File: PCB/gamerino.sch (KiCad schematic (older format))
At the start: 47 parts, among them J1 USB_B_Micro, J2 LT2, J3 RT2, P1 JOY1, P2 JOY2, P3 ICSP, P4 AUX, SW1 HATSWITCH, SW10 OPTS, SW11 X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

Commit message: Update
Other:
- moved on the sheet: J2, JOY1, R4, SW9B
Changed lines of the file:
@@
 	7825 9925 7600 9925
 Wire Wire Line
-	7600 8075 7825 8075
+	7600 8175 7825 8175
 $Comp
 L gamerino-rescue:GND-power #PWR026
@@
 L gamerino-rescue:R-device R4
 U 1 1 60E4EB67
-P 9100 8700
-F 0 "R4" H 9171 8746 50  0000 L CNN
-F 1 "1K" H 9171 8655 50  0000 L CNN
-F 2 "Resistor_SMD:R_0603_1608Metric" V 9030 8700 30  0001 C CNN
-F 3 "" H 9100 8700 30  0000 C CNN
-F 4 "CRG0603F1K0" H 9100 8700 50  0001 C CNN "MPN"
-F 5 "TE" H 9100 8700 50  0001 C CNN "Manufacturer"
-F 6 "A106049CT-ND" H 9100 8700 50  0001 C CNN "Digikey"
-F 7 "279-CRG0603F1K0" H 9100 8700 50  0001 C CNN "Mouser"
-F 8 "213-2266" H 9100 8700 50  0001 C CNN "RS"
-F 9 "3399571" H 9100 8700 50  0001 C CNN "Farnell"
-	1    9100 8700
+P 9100 8800
+F 0 "R4" H 9171 8846 50  0000 L CNN
+F 1 "1K" H 9171 8755 50  0000 L CNN
+F 2 "Resistor_SMD:R_0603_1608Metric" V 9030 8800 30  0001 C CNN
+F 3 "" H 9100 8800 30  0000 C CNN
+F 4 "CRG0603F1K0" H 9100 8800 50  0001 C CNN "MPN"
+F 5 "TE" H 9100 8800 50  0001 C CNN "Manufacturer"
+F 6 "A106049CT-ND" H 9100 8800 50  0001 C CNN "Digikey"
+F 7 "279-CRG0603F1K0" H 9100 8800 50  0001 C CNN "Mouser"
+F 8 "213-2266" H 9100 8800 50  0001 C CNN "RS"
+F 9 "3399571" H 9100 8800 50  0001 C CNN "Farnell"
+	1    9100 8800
 	1    0    0    -1
 $EndComp
@@
 Text Label 10500 4950 0    50   ~ 0
 RT1
-Text Label 7600 8075 2    50   ~ 0
+Text Label 7600 8175 2    50   ~ 0
 LT2
 Text Label 7600 9925 2    50   ~ 0
@@
 L gamerino-rescue:+3.3V-power #PWR023
 U 1 1 6116AC53
-P 7825 7725
-F 0 "#PWR023" H 7825 7575 50  0001 C CNN
-F 1 "+3.3V" H 7840 7898 50  0000 C CNN
-F 2 "" H 7825 7725 50  0001 C CNN
-F 3 "" H 7825 7725 50  0001 C CNN
-	1    7825 7725
+P 7825 7825
+F 0 "#PWR023" H 7825 7675 50  0001 C CNN
+F 1 "+3.3V" H 7840 7998 50  0000 C CNN
+F 2 "" H 7825 7825 50  0001 C CNN
+F 3 "" H 7825 7825 50  0001 C CNN
+	1    7825 7825
 	-1   0    0    -1
 $EndComp
@@
 L gamerino-rescue:GND-power #PWR024
 U 1 1 6116B2BE
-P 7825 8500
-F 0 "#PWR024" H 7825 8250 50  0001 C CNN
-F 1 "GND" H 7830 8327 50  0000 C CNN
-F 2 "" H 7825 8500 50  0001 C CNN
-F 3 "" H 7825 8500 50  0001 C CNN
-	1    7825 8500
+P 7825 8600
+F 0 "#PWR024" H 7825 8350 50  0001 C CNN
+F 1 "GND" H 7830 8427 50  0000 C CNN
+F 2 "" H 7825 8600 50  0001 C CNN
+F 3 "" H 7825 8600 50  0001 C CNN
+	1    7825 8600
 	-1   0    0    -1
 $EndComp
 Wire Wire Line
-	7825 7725 7825 7975
-Wire Wire Line
-	7825 8175 7825 8500
+	7825 7825 7825 8075
+Wire Wire Line
+	7825 8275 7825 8600
 $Comp
 L gamerino-rescue:CONN_3-conn J2
 U 1 1 6116B2CB
-P 8175 8075
-F 0 "J2" H 8042 7739 50  0000 C CNN
-F 1 "LT2" H 8042 7830 50  0000 C CNN
-F 2 "gamerino:Molex_PicoBlade_53047-0310_1x03_P1.25mm_Vertical" H 8175 8075 50  0001 C CNN
-F 3 "" H 8175 8075 50  0001 C CNN
-F 4 "53047-0310" H 8175 8075 50  0001 C CNN "MPN"
-F 5 "Molex" H 8175 8075 50  0001 C CNN "Manufacturer"
-F 6 "WM1732-ND" H 8175 8075 50  0001 C CNN "Digikey"
-F 7 "538-53047-0310" H 8175 8075 50  0001 C CNN "Mouser"
-F 8 "319-1064" H 8175 8075 50  0001 C CNN "RS"
-F 9 "9732853" H 8175 8075 50  0001 C CNN "Farnell"
-	1    8175 8075
+P 8175 8175
+F 0 "J2" H 8042 7839 50  0000 C CNN
+F 1 "LT2" H 8042 7930 50  0000 C CNN
+F 2 "gamerino:Molex_PicoBlade_53047-0310_1x03_P1.25mm_Vertical" H 8175 8175 50  0001 C CNN
+F 3 "" H 8175 8175 50  0001 C CNN
+F 4 "53047-0310" H 8175 8175 50  0001 C CNN "MPN"
+F 5 "Molex" H 8175 8175 50  0001 C CNN "Manufacturer"
+F 6 "WM1732-ND" H 8175 8175 50  0001 C CNN "Digikey"
+F 7 "538-53047-0310" H 8175 8175 50  0001 C CNN "Mouser"
+F 8 "319-1064" H 8175 8175 50  0001 C CNN "RS"
+F 9 "9732853" H 8175 8175 50  0001 C CNN "Farnell"
+	1    8175 8175
 	1    0    0    1
 $EndComp
@@
 Connection ~ 14900 2950
 Wire Wire Line
-	9100 8450 9100 8325
-Wire Wire Line
-	9100 8950 9100 9075
+	9100 8550 9100 8425
+Wire Wire Line
+	9100 9050 9100 9175
 $Comp
 L gamerino-rescue:+3.3V-power #PWR0103
 U 1 1 60C0ACCD
-P 9100 7725
-F 0 "#PWR0103" H 9100 7575 50  0001 C CNN
-F 1 "+3.3V" H 9115 7898 50  0000 C CNN
-F 2 "" H 9100 7725 50  0001 C CNN
-F 3 "" H 9100 7725 50  0001 C CNN
-	1    9100 7725
+P 9100 7825
+F 0 "#PWR0103" H 9100 7675 50  0001 C CNN
+F 1 "+3.3V" H 9115 7998 50  0000 C CNN
+F 2 "" H 9100 7825 50  0001 C CNN
+F 3 "" H 9100 7825 50  0001 C CNN
+	1    9100 7825
 	1    0    0    -1
 $EndComp
@@
 L gamerino:TL1 SW9
 U 2 1 60C5CD0F
-P 8800 8075
-F 0 "SW9" V 8846 7597 50  0000 R CNN
-F 1 "HOME" V 8755 7597 50  0000 R CNN
-F 2 "gamerino:TL3265" H 8800 8225 50  0001 C CNN
-F 3 "" H 8800 8225 50  0001 C CNN
-F 4 "TL3265GQSCLR" H 8800 8075 50  0001 C CNN "MPN"
-F 5 "E-Switch" H 8800 8075 50  0001 C CNN "Manufacturer"
-F 6 "EG5518CT-ND" H 8800 8075 50  0001 C CNN "Digikey"
-F 7 "612-TL3265GQSCLR" H 8800 8075 50  0001 C CNN "Mouser"
-	2    8800 8075
+P 8800 8175
+F 0 "SW9" V 8846 7697 50  0000 R CNN
+F 1 "HOME" V 8755 7697 50  0000 R CNN
+F 2 "gamerino:TL3265" H 8800 8325 50  0001 C CNN
+F 3 "" H 8800 8325 50  0001 C CNN
+F 4 "TL3265GQSCLR" H 8800 8175 50  0001 C CNN "MPN"
+F 5 "E-Switch" H 8800 8175 50  0001 C CNN "Manufacturer"
+F 6 "EG5518CT-ND" H 8800 8175 50  0001 C CNN "Digikey"
+F 7 "612-TL3265GQSCLR" H 8800 8175 50  0001 C CNN "Mouser"
+	2    8800 8175
 	0    -1   -1   0
 $EndComp
 Wire Wire Line
-	9100 7825 9100 7725
+	9100 7925 9100 7825
 Wire Wire Line
 	14725 4325 14900 4325
@@
 L gamerino:RKJXU JOY1
 U 1 1 60AED526
-P 10725 7975
-F 0 "JOY1" H 10650 8400 50  0000 C CNN
-F 1 "RKJXU" H 10650 8300 50  0000 C CNN
-F 2 "gamerino:RKJXU" H 10050 7975 50  0001 C CNN
-F 3 "" H 10050 7975 50  0001 C CNN
-F 4 "RKJXU1210006" H 10725 7975 50  0001 C CNN "MPN"
-F 5 "ALPS Alpine" H 10725 7975 50  0001 C CNN "Manufacturer"
-F 6 "688-RKJXU1210006" H 10725 7975 50  0001 C CNN "Mouser"
-	1    10725 7975
+P 10725 8050
+F 0 "JOY1" H 10650 8475 50  0000 C CNN
+F 1 "RKJXU" H 10650 8375 50  0000 C CNN
+F 2 "gamerino:RKJXU" H 10050 8050 50  0001 C CNN
+F 3 "" H 10050 8050 50  0001 C CNN
+F 4 "RKJXU1210006" H 10725 8050 50  0001 C CNN "MPN"
+F 5 "ALPS Alpine" H 10725 8050 50  0001 C CNN "Manufacturer"
+F 6 "688-RKJXU1210006" H 10725 8050 50  0001 C CNN "Mouser"
+	1    10725 8050
 	1    0    0    -1
 $EndComp
@@
 NoConn ~ 10925 10300
 NoConn ~ 11200 9600
-NoConn ~ 11200 7750
-NoConn ~ 10050 7975
-NoConn ~ 10050 8175
-NoConn ~ 10925 8450
-Wire Wire Line
-	9100 9075 8900 9075
-Text Label 8900 9075 2    50   ~ 0
+NoConn ~ 11200 7825
+NoConn ~ 10050 8050
+NoConn ~ 10050 8250
+NoConn ~ 10925 8525
+Wire Wire Line
+	9100 9175 8900 9175
+Text Label 8900 9175 2    50   ~ 0
 LHOME
 Text Label 4725 4550 0    50   ~ 0

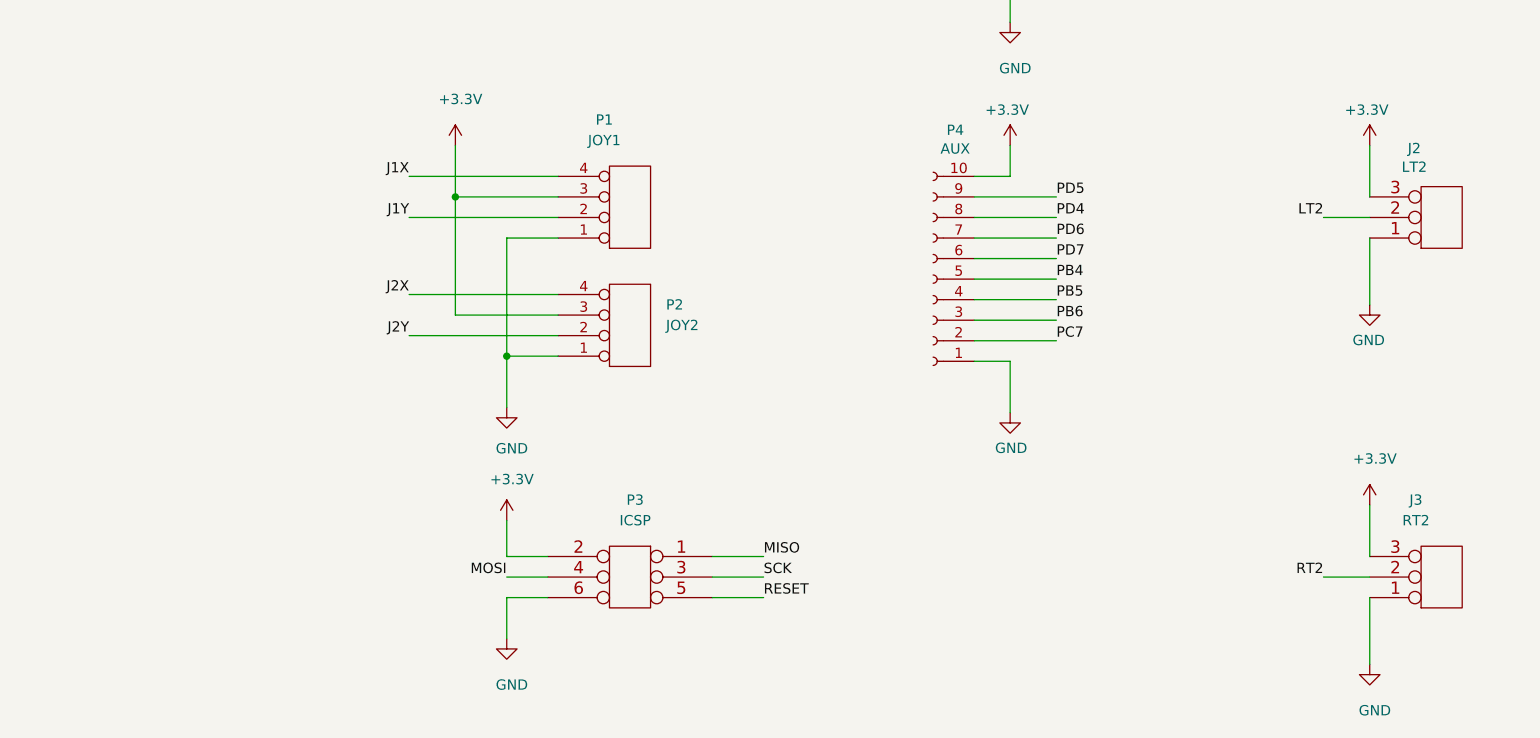
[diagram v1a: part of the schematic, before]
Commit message: Add ESD protections to analog inputs
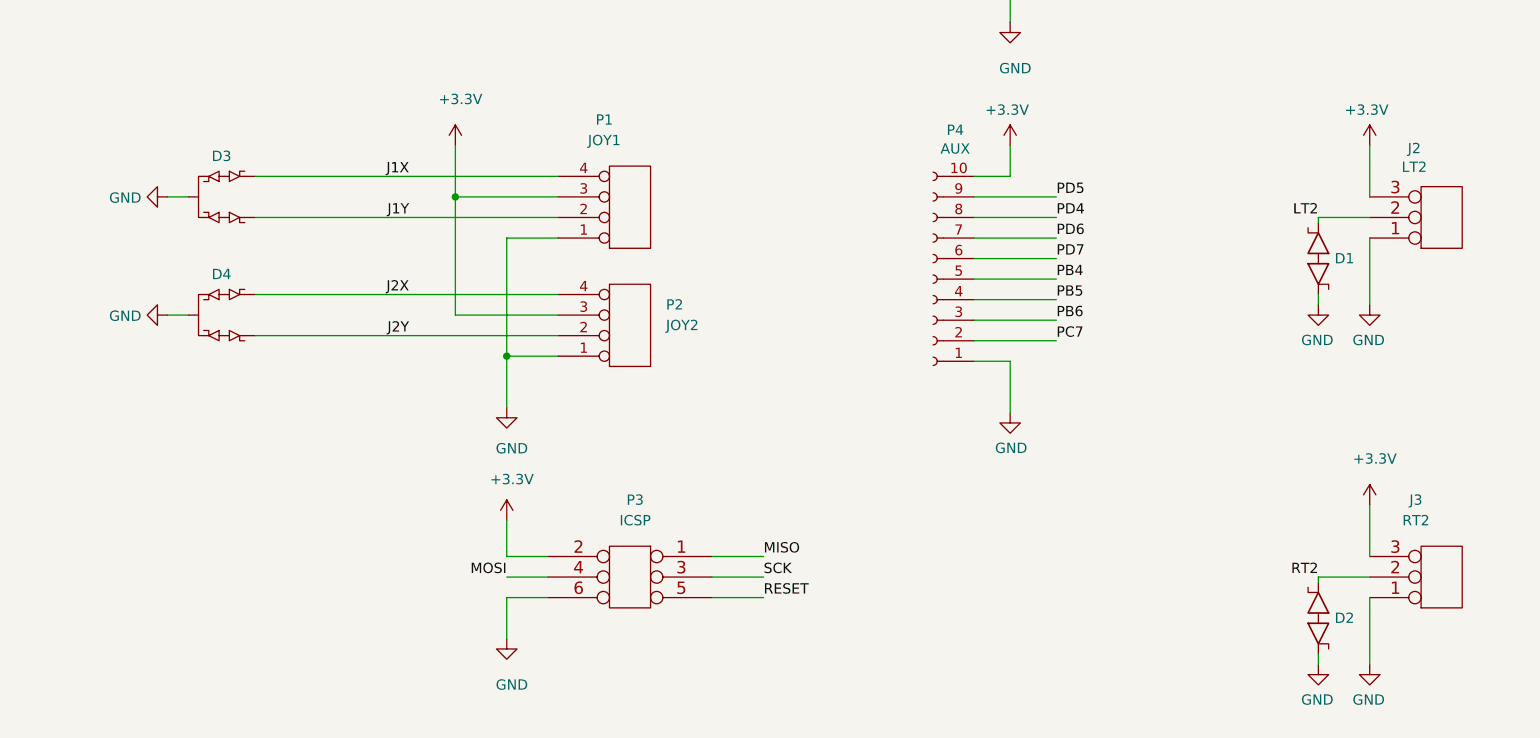
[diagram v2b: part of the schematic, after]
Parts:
- added D1, D2: TRANSIL, symbol gamerino:TRANSIL
- added D3, D4: D5V0L2B3W, Package_TO_SOT_SMD:SOT-323_SC-70, symbol gamerino:TRANSIL2
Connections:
- net GND: now also D1.2 (A2), D2.2 (A2), D3.3, D4.3
- net J1X: now also D3.1
- net J1Y: now also D3.2
- net J2X: now also D4.1
- net J2Y: now also D4.2
- net LT2: now also D1.1 (A1)
- net RT2: now also D2.1 (A1)
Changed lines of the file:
@@
 Wire Wire Line
 	3375 8075 3875 8075
-Wire Wire Line
-	3875 8175 3150 8175
-Wire Wire Line
-	3875 7975 3150 7975
-Wire Wire Line
-	3875 8550 3150 8550
-Wire Wire Line
-	3875 8750 3150 8750
 $Comp
 L gamerino:RKJXS SW1
@@
 	10325 4750 10500 4750
 Wire Wire Line
-	7825 9925 7600 9925
-Wire Wire Line
-	7600 8175 7825 8175
+	7825 9925 7575 9925
 $Comp
 L gamerino-rescue:GND-power #PWR026
@@
 P 7825 10350
 F 0 "#PWR026" H 7825 10100 50  0001 C CNN
-F 1 "GND" H 7800 10125 50  0000 C CNN
+F 1 "GND" H 7830 10177 50  0000 C CNN
 F 2 "" H 7825 10350 50  0001 C CNN
 F 3 "" H 7825 10350 50  0001 C CNN
@@
 Text Label 10500 4950 0    50   ~ 0
 RT1
-Text Label 7600 8175 2    50   ~ 0
+Text Label 7575 8175 2    50   ~ 0
 LT2
-Text Label 7600 9925 2    50   ~ 0
+Text Label 7575 9925 2    50   ~ 0
 RT2
 Text Label 3150 7975 2    50   ~ 0
@@
 Wire Wire Line
 	14900 2675 14900 2950
+$Comp
+L gamerino-rescue:GND-power #PWR0102
+U 1 1 60B381A8
+P 7575 8600
+F 0 "#PWR0102" H 7575 8350 50  0001 C CNN
+F 1 "GND" H 7580 8427 50  0000 C CNN
+F 2 "" H 7575 8600 50  0001 C CNN
+F 3 "" H 7575 8600 50  0001 C CNN
+	1    7575 8600
+	-1   0    0    -1
+$EndComp
+Wire Wire Line
+	7575 8175 7825 8175
+$Comp
+L gamerino-rescue:GND-power #PWR0104
+U 1 1 60B5F501
+P 7575 10350
+F 0 "#PWR0104" H 7575 10100 50  0001 C CNN
+F 1 "GND" H 7580 10177 50  0000 C CNN
+F 2 "" H 7575 10350 50  0001 C CNN
+F 3 "" H 7575 10350 50  0001 C CNN
+	1    7575 10350
+	-1   0    0    -1
+$EndComp
+Wire Wire Line
+	7575 9925 7575 9950
+Wire Wire Line
+	7575 8175 7575 8200
+$Comp
+L gamerino:TRANSIL D1
+U 1 1 60BC29DD
+P 7575 8375
+F 0 "D1" V 7575 8454 50  0000 L CNN
+F 1 "TRANSIL" H 7575 8275 50  0001 C CNN
+F 2 "" H 7425 8175 50  0001 C CNN
+F 3 "" H 7425 8375 50  0001 C CNN
+F 4 "Nexperia" H 7575 8375 50  0001 C CNN "Manufacturer"
+	1    7575 8375
+	0    1    1    0
+$EndComp
+Wire Wire Line
+	7575 8600 7575 8550
+$Comp
+L gamerino:TRANSIL D2
+U 1 1 60C18431
+P 7575 10125
+F 0 "D2" V 7575 10204 50  0000 L CNN
+F 1 "TRANSIL" H 7575 10025 50  0001 C CNN
+F 2 "" H 7425 9925 50  0001 C CNN
+F 3 "" H 7425 10125 50  0001 C CNN
+F 4 "Nexperia" H 7575 10125 50  0001 C CNN "Manufacturer"
+	1    7575 10125
+	0    1    1    0
+$EndComp
+Wire Wire Line
+	7575 10300 7575 10350
+$Comp
+L gamerino:TRANSIL2 D3
+U 1 1 60C500FC
+P 2250 8075
+F 0 "D3" H 2263 8273 50  0000 C CNN
+F 1 "D5V0L2B3W" V 2307 8203 50  0001 L CNN
+F 2 "Package_TO_SOT_SMD:SOT-323_SC-70" H 2150 8275 50  0001 C CNN
+F 3 "" H 2150 8275 50  0001 C CNN
+F 4 "D5V0L2B3W-7DICT-ND" H 2250 8075 50  0001 C CNN "Digikey"
+F 5 "3127275" H 2250 8075 50  0001 C CNN "Farnell"
+F 6 "D5V0L2B3W" H 2250 8075 50  0001 C CNN "MPN"
+F 7 "Diodes" H 2250 8075 50  0001 C CNN "Manufacturer"
+F 8 "621-D5V0L2B3W-7" H 2250 8075 50  0001 C CNN "Mouser"
+F 9 "770-4780" H 2250 8075 50  0001 C CNN "RS"
+	1    2250 8075
+	-1   0    0    -1
+$EndComp
+$Comp
+L gamerino-rescue:GND-power #PWR0105
+U 1 1 60C509D2
+P 1975 8075
+F 0 "#PWR0105" H 1975 7825 50  0001 C CNN
+F 1 "GND" V 1980 7947 50  0000 R CNN
+F 2 "" H 1975 8075 50  0001 C CNN
+F 3 "" H 1975 8075 50  0001 C CNN
+	1    1975 8075
+	0    1    1    0
+$EndComp
+Wire Wire Line
+	2075 8075 1975 8075
+Wire Wire Line
+	2075 8650 1975 8650
+$Comp
+L gamerino-rescue:GND-power #PWR0106
+U 1 1 60C82F9E
+P 1975 8650
+F 0 "#PWR0106" H 1975 8400 50  0001 C CNN
+F 1 "GND" V 1980 8522 50  0000 R CNN
+F 2 "" H 1975 8650 50  0001 C CNN
+F 3 "" H 1975 8650 50  0001 C CNN
+	1    1975 8650
+	0    1    1    0
+$EndComp
+Wire Wire Line
+	2400 8175 3875 8175
+Wire Wire Line
+	2400 7975 3875 7975
+Wire Wire Line
+	2400 8750 3875 8750
+Wire Wire Line
+	2400 8550 3875 8550
+$Comp
+L gamerino:TRANSIL2 D4
+U 1 1 60EFC609
+P 2250 8650
+F 0 "D4" H 2263 8848 50  0000 C CNN
+F 1 "D5V0L2B3W" V 2307 8778 50  0001 L CNN
+F 2 "Package_TO_SOT_SMD:SOT-323_SC-70" H 2150 8850 50  0001 C CNN
+F 3 "" H 2150 8850 50  0001 C CNN
+F 4 "D5V0L2B3W-7DICT-ND" H 2250 8650 50  0001 C CNN "Digikey"
+F 5 "3127275" H 2250 8650 50  0001 C CNN "Farnell"
+F 6 "D5V0L2B3W" H 2250 8650 50  0001 C CNN "MPN"
+F 7 "Diodes" H 2250 8650 50  0001 C CNN "Manufacturer"
+F 8 "621-D5V0L2B3W-7" H 2250 8650 50  0001 C CNN "Mouser"
+F 9 "770-4780" H 2250 8650 50  0001 C CNN "RS"
+	1    2250 8650
+	-1   0    0    -1
+$EndComp
 $EndSCHEMATC

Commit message: Update BOM
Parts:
- D1, D2: value TRANSIL -> PESD5V0U1BBYL; footprint (none) -> Diode_SMD:D_SOD-523; Digikey (none) -> 1727-8532-1-ND; Farnell (none) -> 2114879; MPN (none) -> PESD5V0U1BBYL; Mouser (none) -> 771-PESD5V0U1BBT/R; RS (none) -> 725-8723
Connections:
- net J1X: now also D3.2; no longer D3.1
- net J1Y: no longer D3.2
- net J2X: now also D4.2; no longer D4.1
- net J2Y: now also D3.1, D4.1; no longer D4.2
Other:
- moved on the sheet: D3, D4
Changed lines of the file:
@@
 Text Label 7575 9925 2    50   ~ 0
 RT2
-Text Label 3150 7975 2    50   ~ 0
+Text Label 2400 7975 2    50   ~ 0
 J1X
-Text Label 3150 8175 2    50   ~ 0
+Text Label 2400 8175 2    50   ~ 0
 J1Y
-Text Label 3150 8550 2    50   ~ 0
+Text Label 2400 8550 2    50   ~ 0
 J2X
-Text Label 3150 8750 2    50   ~ 0
+Text Label 2400 8750 2    50   ~ 0
 J2Y
 Text Label 3625 9925 2    50   ~ 0
@@
 P 7575 8375
 F 0 "D1" V 7575 8454 50  0000 L CNN
-F 1 "TRANSIL" H 7575 8275 50  0001 C CNN
-F 2 "" H 7425 8175 50  0001 C CNN
+F 1 "PESD5V0U1BBYL" H 7575 8275 50  0001 C CNN
+F 2 "Diode_SMD:D_SOD-523" H 7425 8175 50  0001 C CNN
 F 3 "" H 7425 8375 50  0001 C CNN
 F 4 "Nexperia" H 7575 8375 50  0001 C CNN "Manufacturer"
+F 5 "1727-8532-1-ND" H 7575 8375 50  0001 C CNN "Digikey"
+F 6 "2114879" H 7575 8375 50  0001 C CNN "Farnell"
+F 7 "PESD5V0U1BBYL" H 7575 8375 50  0001 C CNN "MPN"
+F 8 "771-PESD5V0U1BBT/R" H 7575 8375 50  0001 C CNN "Mouser"
+F 9 "725-8723" H 7575 8375 50  0001 C CNN "RS"
 	1    7575 8375
 	0    1    1    0
@@
 P 7575 10125
 F 0 "D2" V 7575 10204 50  0000 L CNN
-F 1 "TRANSIL" H 7575 10025 50  0001 C CNN
-F 2 "" H 7425 9925 50  0001 C CNN
+F 1 "PESD5V0U1BBYL" H 7575 10025 50  0001 C CNN
+F 2 "Diode_SMD:D_SOD-523" H 7425 9925 50  0001 C CNN
 F 3 "" H 7425 10125 50  0001 C CNN
 F 4 "Nexperia" H 7575 10125 50  0001 C CNN "Manufacturer"
+F 5 "1727-8532-1-ND" H 7575 10125 50  0001 C CNN "Digikey"
+F 6 "2114879" H 7575 10125 50  0001 C CNN "Farnell"
+F 7 "PESD5V0U1BBYL" H 7575 10125 50  0001 C CNN "MPN"
+F 8 "771-PESD5V0U1BBT/R" H 7575 10125 50  0001 C CNN "Mouser"
+F 9 "725-8723" H 7575 10125 50  0001 C CNN "RS"
 	1    7575 10125
 	0    1    1    0
@@
 L gamerino:TRANSIL2 D3
 U 1 1 60C500FC
-P 2250 8075
-F 0 "D3" H 2263 8273 50  0000 C CNN
-F 1 "D5V0L2B3W" V 2307 8203 50  0001 L CNN
-F 2 "Package_TO_SOT_SMD:SOT-323_SC-70" H 2150 8275 50  0001 C CNN
-F 3 "" H 2150 8275 50  0001 C CNN
-F 4 "D5V0L2B3W-7DICT-ND" H 2250 8075 50  0001 C CNN "Digikey"
-F 5 "3127275" H 2250 8075 50  0001 C CNN "Farnell"
-F 6 "D5V0L2B3W" H 2250 8075 50  0001 C CNN "MPN"
-F 7 "Diodes" H 2250 8075 50  0001 C CNN "Manufacturer"
-F 8 "621-D5V0L2B3W-7" H 2250 8075 50  0001 C CNN "Mouser"
-F 9 "770-4780" H 2250 8075 50  0001 C CNN "RS"
-	1    2250 8075
-	-1   0    0    -1
+P 3075 8950
+F 0 "D3" V 3087 8797 50  0000 R CNN
+F 1 "D5V0L2B3W" V 3132 9078 50  0001 L CNN
+F 2 "Package_TO_SOT_SMD:SOT-323_SC-70" H 2975 9150 50  0001 C CNN
+F 3 "" H 2975 9150 50  0001 C CNN
+F 4 "D5V0L2B3W-7DICT-ND" H 3075 8950 50  0001 C CNN "Digikey"
+F 5 "3127275" H 3075 8950 50  0001 C CNN "Farnell"
+F 6 "D5V0L2B3W" H 3075 8950 50  0001 C CNN "MPN"
+F 7 "Diodes" H 3075 8950 50  0001 C CNN "Manufacturer"
+F 8 "621-D5V0L2B3W-7" H 3075 8950 50  0001 C CNN "Mouser"
+F 9 "770-4780" H 3075 8950 50  0001 C CNN "RS"
+	1    3075 8950
+	0    -1   1    0
 $EndComp
 $Comp
 L gamerino-rescue:GND-power #PWR0105
 U 1 1 60C509D2
-P 1975 8075
-F 0 "#PWR0105" H 1975 7825 50  0001 C CNN
-F 1 "GND" V 1980 7947 50  0000 R CNN
-F 2 "" H 1975 8075 50  0001 C CNN
-F 3 "" H 1975 8075 50  0001 C CNN
-	1    1975 8075
-	0    1    1    0
-$EndComp
-Wire Wire Line
-	2075 8075 1975 8075
-Wire Wire Line
-	2075 8650 1975 8650
+P 3075 9225
+F 0 "#PWR0105" H 3075 8975 50  0001 C CNN
+F 1 "GND" H 3080 9052 50  0000 C CNN
+F 2 "" H 3075 9225 50  0001 C CNN
+F 3 "" H 3075 9225 50  0001 C CNN
+	1    3075 9225
+	1    0    0    -1
+$EndComp
+Wire Wire Line
+	3075 9125 3075 9225
+Wire Wire Line
+	2675 9125 2675 9225
 $Comp
 L gamerino-rescue:GND-power #PWR0106
 U 1 1 60C82F9E
-P 1975 8650
-F 0 "#PWR0106" H 1975 8400 50  0001 C CNN
-F 1 "GND" V 1980 8522 50  0000 R CNN
-F 2 "" H 1975 8650 50  0001 C CNN
-F 3 "" H 1975 8650 50  0001 C CNN
-	1    1975 8650
-	0    1    1    0
+P 2675 9225
+F 0 "#PWR0106" H 2675 8975 50  0001 C CNN
+F 1 "GND" H 2680 9052 50  0000 C CNN
+F 2 "" H 2675 9225 50  0001 C CNN
+F 3 "" H 2675 9225 50  0001 C CNN
+	1    2675 9225
+	1    0    0    -1
 $EndComp
 Wire Wire Line
 	2400 8175 3875 8175
 Wire Wire Line
-	2400 7975 3875 7975
-Wire Wire Line
-	2400 8750 3875 8750
-Wire Wire Line
-	2400 8550 3875 8550
+	2400 7975 3175 7975
+Wire Wire Line
+	2400 8750 2575 8750
+Wire Wire Line
+	2400 8550 2775 8550
 $Comp
 L gamerino:TRANSIL2 D4
 U 1 1 60EFC609
-P 2250 8650
-F 0 "D4" H 2263 8848 50  0000 C CNN
-F 1 "D5V0L2B3W" V 2307 8778 50  0001 L CNN
-F 2 "Package_TO_SOT_SMD:SOT-323_SC-70" H 2150 8850 50  0001 C CNN
-F 3 "" H 2150 8850 50  0001 C CNN
-F 4 "D5V0L2B3W-7DICT-ND" H 2250 8650 50  0001 C CNN "Digikey"
-F 5 "3127275" H 2250 8650 50  0001 C CNN "Farnell"
-F 6 "D5V0L2B3W" H 2250 8650 50  0001 C CNN "MPN"
-F 7 "Diodes" H 2250 8650 50  0001 C CNN "Manufacturer"
-F 8 "621-D5V0L2B3W-7" H 2250 8650 50  0001 C CNN "Mouser"
-F 9 "770-4780" H 2250 8650 50  0001 C CNN "RS"
-	1    2250 8650
-	-1   0    0    -1
-$EndComp
+P 2675 8950
+F 0 "D4" V 2687 8797 50  0000 R CNN
+F 1 "D5V0L2B3W" V 2732 9078 50  0001 L CNN
+F 2 "Package_TO_SOT_SMD:SOT-323_SC-70" H 2575 9150 50  0001 C CNN
+F 3 "" H 2575 9150 50  0001 C CNN
+F 4 "D5V0L2B3W-7DICT-ND" H 2675 8950 50  0001 C CNN "Digikey"
+F 5 "3127275" H 2675 8950 50  0001 C CNN "Farnell"
+F 6 "D5V0L2B3W" H 2675 8950 50  0001 C CNN "MPN"
+F 7 "Diodes" H 2675 8950 50  0001 C CNN "Manufacturer"
+F 8 "621-D5V0L2B3W-7" H 2675 8950 50  0001 C CNN "Mouser"
+F 9 "770-4780" H 2675 8950 50  0001 C CNN "RS"
+	1    2675 8950
+	0    -1   1    0
+$EndComp
+Wire Wire Line
+	2575 8800 2575 8750
+Connection ~ 2575 8750
+Wire Wire Line
+	2575 8750 2975 8750
+Wire Wire Line
+	2775 8800 2775 8550
+Connection ~ 2775 8550
+Wire Wire Line
+	2775 8550 3875 8550
+Wire Wire Line
+	2975 8800 2975 8750
+Connection ~ 2975 8750
+Wire Wire Line
+	2975 8750 3875 8750
+Wire Wire Line
+	3175 8800 3175 7975
+Connection ~ 3175 7975
+Wire Wire Line
+	3175 7975 3875 7975
 $EndSCHEMATC
